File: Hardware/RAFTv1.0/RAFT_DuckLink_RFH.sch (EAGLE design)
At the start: 144 parts, among them J1 AMPHENOL_132134, J2 AMPHENOL_132134, J4 Micro-USB, J5 132134-15, J6 S2B-PH-K-S(LF)(SN), Q1 SIA817EDJ, Q2 SI7288DP, Q4 SI7288DP, U1 SX1276, U10 PE4259, U2 MAX2771ETI+, U3 ESP32-D0WD, U4 W25Q16BVSSIG, U5 INTERFACE-CP2102-GMR(QFN28), U6 PE4259, U7 SP0503BAHT, U8 BQ24650RVAR, U9 TPS63070RNMT, Y1 32.768kHz

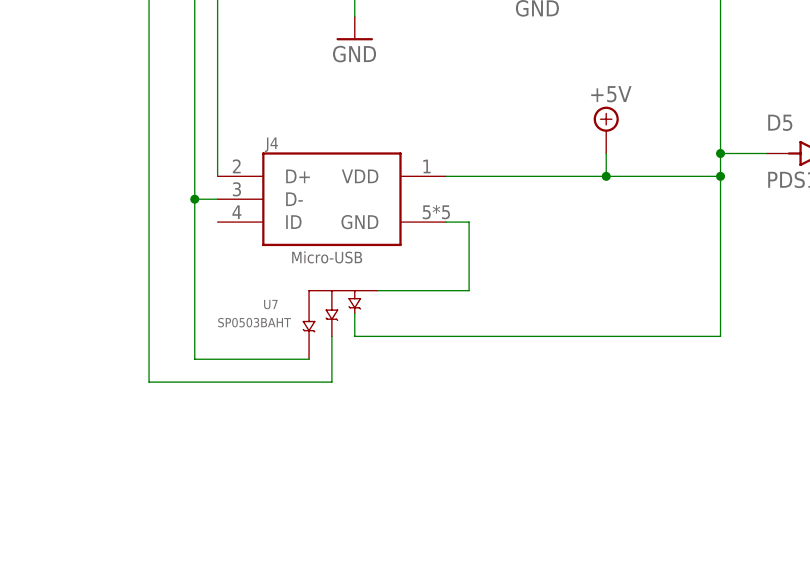
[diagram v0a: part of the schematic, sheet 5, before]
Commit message: added uart to board layout
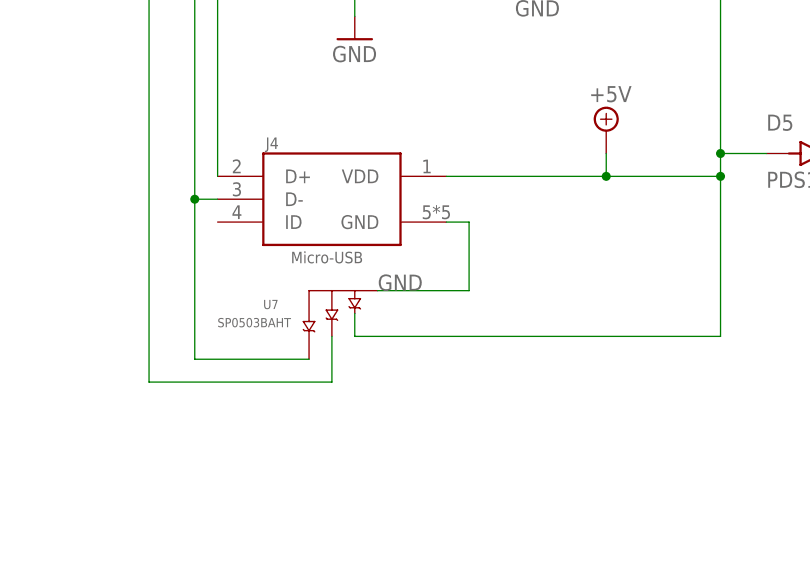
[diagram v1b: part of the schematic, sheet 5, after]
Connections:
- removed net N$56: J4.GND, U7.GND
- net GND: now also J4.GND, U7.GND
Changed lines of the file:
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@@
 <pinref part="R9" gate="G$1" pin="2"/>
+</segment>
+<segment>
+<pinref part="J4" gate="G$1" pin="GND"/>
+<wire x1="-2.54" y1="-38.1" x2="0" y2="-38.1" width="0.1524" layer="91"/>
+<pinref part="U7" gate="G$1" pin="GND"/>
+<wire x1="0" y1="-38.1" x2="0" y2="-45.72" width="0.1524" layer="91"/>
+<wire x1="0" y1="-45.72" x2="-10.16" y2="-45.72" width="0.1524" layer="91"/>
+<label x="-10.16" y="-45.72" size="1.778" layer="95"/>
 </segment>
 </net>
@@
 </segment>
 </net>
-<net name="N$56" class="0">
-<segment>
-<pinref part="J4" gate="G$1" pin="GND"/>
-<wire x1="-2.54" y1="-38.1" x2="0" y2="-38.1" width="0.1524" layer="91"/>
-<pinref part="U7" gate="G$1" pin="GND"/>
-<wire x1="0" y1="-38.1" x2="0" y2="-45.72" width="0.1524" layer="91"/>
-<wire x1="0" y1="-45.72" x2="-10.16" y2="-45.72" width="0.1524" layer="91"/>
-</segment>
-</net>

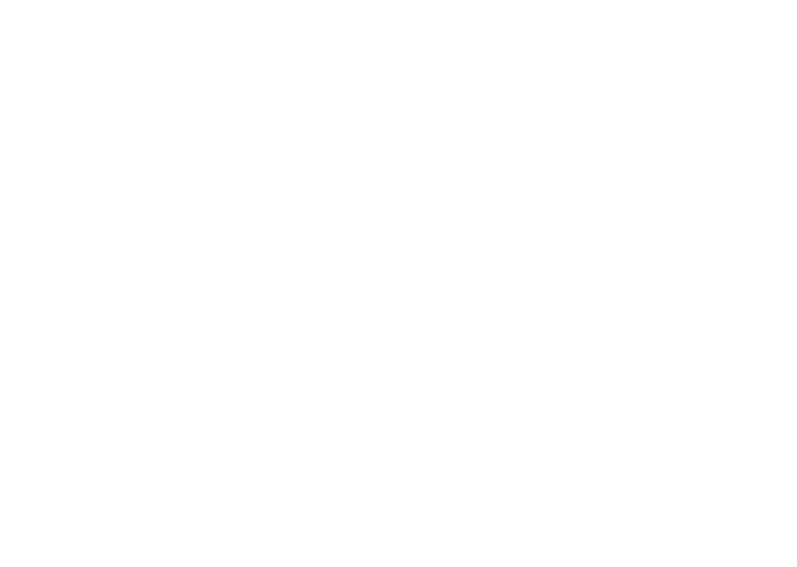
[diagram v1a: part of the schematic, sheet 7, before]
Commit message: added barrel jack. generated new PDFs
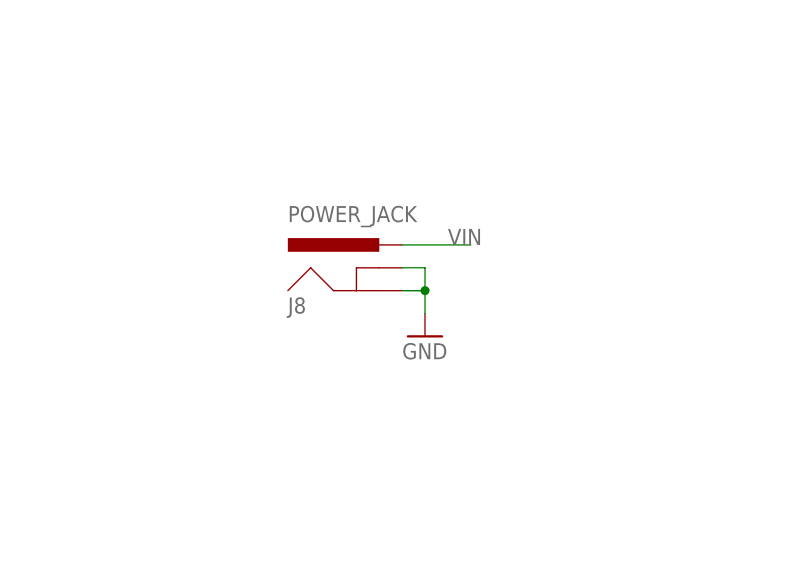
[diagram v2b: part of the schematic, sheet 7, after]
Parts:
- added J8: POWER_JACK, SparkFun-Connectors:POWER_JACK
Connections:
- net GND: now also J8.GND, J8.GNDBREAK
- net VIN: now also J8.PWR
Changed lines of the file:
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@@
 <part name="GND89" library="supply1" library_urn="urn:adsk.eagle:library:371" deviceset="GND" device=""/>
 <part name="D6" library="WL-SMCW" deviceset="WL-SMCW" device="-150060BS75000-B" value="150060RS75000"/>
+<part name="J8" library="SparkFun-Connectors" deviceset="POWER_JACK" device=""/>
+<part name="GND90" library="supply1" library_urn="urn:adsk.eagle:library:371" deviceset="GND" device=""/>
 </parts>
 <sheets>
@@
 </instance>
 <instance part="R14" gate="G$1" x="-104.14" y="33.02" smashed="yes" rot="R90">
-<attribute name="NAME" x="-97.277559375" y="36.06651875" size="2.54148125" layer="95" rot="R180"/>
-<attribute name="VALUE" x="-97.52603125" y="32.772640625" size="2.54331875" layer="96" rot="R180"/>
+<attribute name="NAME" x="-100.842440625" y="29.97348125" size="2.54148125" layer="95"/>
+<attribute name="VALUE" x="-100.59396875" y="33.267359375" size="2.54331875" layer="96"/>
 </instance>
 <instance part="R15" gate="G$1" x="-30.48" y="33.02" smashed="yes">
@@
 <attribute name="VALUE" x="45.72" y="38.1" size="1.778" layer="96"/>
 </instance>
+<instance part="J8" gate="G$1" x="-63.5" y="-55.88" smashed="yes">
+<attribute name="VALUE" x="-73.66" y="-45.72" size="1.778" layer="96" font="vector"/>
+<attribute name="NAME" x="-73.66" y="-55.88" size="1.778" layer="95" font="vector"/>
+</instance>
+<instance part="GND90" gate="1" x="-58.42" y="-58.42" smashed="yes">
+<attribute name="VALUE" x="-60.96" y="-60.96" size="1.778" layer="96"/>
+</instance>
 </instances>
 <busses>
@@
 <wire x1="71.12" y1="43.18" x2="48.26" y2="43.18" width="0.1524" layer="91"/>
 </segment>
+<segment>
+<pinref part="J8" gate="G$1" pin="GND"/>
+<pinref part="GND90" gate="1" pin="GND"/>
+<wire x1="-60.96" y1="-53.34" x2="-58.42" y2="-53.34" width="0.1524" layer="91"/>
+<wire x1="-58.42" y1="-53.34" x2="-58.42" y2="-55.88" width="0.1524" layer="91"/>
+<pinref part="J8" gate="G$1" pin="GNDBREAK"/>
+<wire x1="-60.96" y1="-50.8" x2="-58.42" y2="-50.8" width="0.1524" layer="91"/>
+<wire x1="-58.42" y1="-50.8" x2="-58.42" y2="-53.34" width="0.1524" layer="91"/>
+<junction x="-58.42" y="-53.34"/>
+</segment>
 </net>
 <net name="RTS" class="0">
@@
 </segment>
 </net>
+<net name="VIN" class="0">
+<segment>
+<pinref part="J8" gate="G$1" pin="PWR"/>
+<wire x1="-60.96" y1="-48.26" x2="-53.34" y2="-48.26" width="0.1524" layer="91"/>
+<label x="-55.88" y="-48.26" size="1.778" layer="95"/>
+</segment>
+</net>

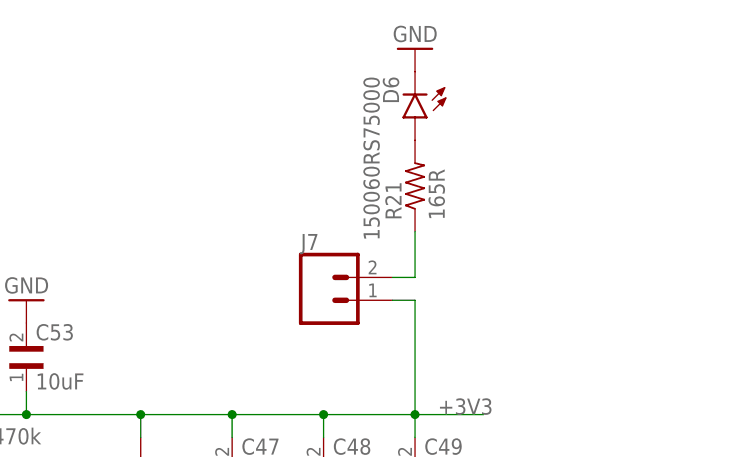
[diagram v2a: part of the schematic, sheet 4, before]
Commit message: battery charger/power distribution layouts
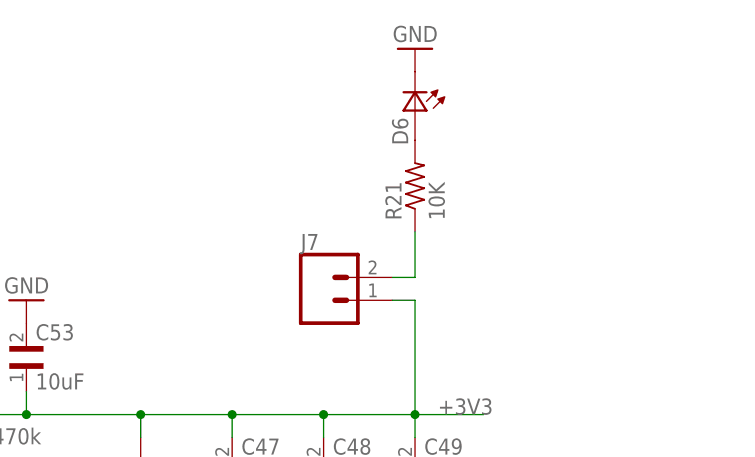
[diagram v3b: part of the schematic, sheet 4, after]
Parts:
- D6: value 150060RS75000 -> LTST-C190GKT; device WL-SMCW:WL-SMCW-150060BS75000-B -> LTST-C190GKT:LTST-C190GKT
- R21: value 165R -> 10K; device RAFT-components:CRCW1206165RFKEA -> CRCW040210K0JNED:CRCW040210K0JNED
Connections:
- net GND: now also D6.K2; no longer D6.C
- net N$52: now also D6.A2; no longer D6.A
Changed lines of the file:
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@@
 <part name="GND88" library="supply1" library_urn="urn:adsk.eagle:library:371" deviceset="GND" device=""/>
 <part name="J7" library="SparkFun-Connectors" deviceset="CONN_02" device=""/>
-<part name="R21" library="RAFT-components" deviceset="CRCW1206165RFKEA" device="" value="165R"/>
 <part name="GND89" library="supply1" library_urn="urn:adsk.eagle:library:371" deviceset="GND" device=""/>
-<part name="D6" library="WL-SMCW" deviceset="WL-SMCW" device="-150060BS75000-B" value="150060RS75000"/>
 <part name="J8" library="SparkFun-Connectors" deviceset="POWER_JACK" device=""/>
 <part name="GND90" library="supply1" library_urn="urn:adsk.eagle:library:371" deviceset="GND" device=""/>
+<part name="R21" library="CRCW040210K0JNED" deviceset="CRCW040210K0JNED" device="" value="10K"/>
+<part name="D6" library="LTST-C190GKT" deviceset="LTST-C190GKT" device=""/>
 </parts>
 <sheets>
@@
 <attribute name="NAME" x="71.12" y="28.448" size="1.778" layer="95" font="vector"/>
 </instance>
+<instance part="GND89" gate="1" x="83.82" y="50.8" smashed="yes" rot="R180">
+<attribute name="VALUE" x="86.36" y="53.34" size="1.778" layer="96" rot="R180"/>
+</instance>
 <instance part="R21" gate="G$1" x="83.82" y="35.56" smashed="yes" rot="R90">
 <attribute name="NAME" x="82.3214" y="31.75" size="1.778" layer="95" rot="R90"/>
 <attribute name="VALUE" x="87.122" y="31.75" size="1.778" layer="96" rot="R90"/>
 </instance>
-<instance part="GND89" gate="1" x="83.82" y="50.8" smashed="yes" rot="R180">
-<attribute name="VALUE" x="86.36" y="53.34" size="1.778" layer="96" rot="R180"/>
-</instance>
-<instance part="D6" gate="G$1" x="83.82" y="43.18" smashed="yes" rot="R180">
-<attribute name="NAME" x="80.264" y="47.752" size="1.778" layer="95" rot="R270"/>
-<attribute name="VALUE" x="78.105" y="47.752" size="1.778" layer="96" rot="R270"/>
+<instance part="D6" gate="G$1" x="83.82" y="45.72" smashed="yes" rot="R180">
+<attribute name="NAME" x="81.28203125" y="43.17796875" size="1.77941875" layer="95" rot="R270"/>
 </instance>
 </instances>
@@
 </segment>
 <segment>
+<pinref part="D6" gate="G$1" pin="K2"/>
 <pinref part="GND89" gate="1" pin="GND"/>
-<pinref part="D6" gate="G$1" pin="C"/>
 </segment>
 </net>
@@
 <pinref part="J7" gate="G$1" pin="2"/>
 <wire x1="81.28" y1="25.4" x2="83.82" y2="25.4" width="0.1524" layer="91"/>
+<wire x1="83.82" y1="25.4" x2="83.82" y2="30.48" width="0.1524" layer="91"/>
 <pinref part="R21" gate="G$1" pin="1"/>
-<wire x1="83.82" y1="25.4" x2="83.82" y2="30.48" width="0.1524" layer="91"/>
 </segment>
 </net>
 <net name="N$52" class="0">
 <segment>
+<pinref part="D6" gate="G$1" pin="A2"/>
 <pinref part="R21" gate="G$1" pin="2"/>
-<pinref part="D6" gate="G$1" pin="A"/>
-</segment>
-</net>
+</segment>
+</net>

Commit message: preliminary board layout
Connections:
- net 2G4_INT_ANT: now also U10.RF2; no longer U10.RF1
- net N$70: now also U10.RF1; no longer U10.RF2
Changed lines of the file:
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@@
-</segment>
-</net>
-<net name="2G4_INT_ANT" class="0">
-<segment>
-<wire x1="-190.5" y1="-50.8" x2="-213.36" y2="-50.8" width="0.1524" layer="91"/>
-<label x="-213.36" y="-50.8" size="1.778" layer="95"/>
-<pinref part="U10" gate="G$1" pin="RF1"/>
 </segment>
 </net>
@@
 <net name="N$70" class="0">
 <segment>
-<wire x1="-190.5" y1="-53.34" x2="-195.58" y2="-53.34" width="0.1524" layer="91"/>
-<wire x1="-195.58" y1="-53.34" x2="-195.58" y2="-58.42" width="0.1524" layer="91"/>
 <pinref part="J5" gate="G$1" pin="SIG"/>
 <wire x1="-195.58" y1="-58.42" x2="-205.74" y2="-58.42" width="0.1524" layer="91"/>
-<pinref part="U10" gate="G$1" pin="RF2"/>
+<pinref part="U10" gate="G$1" pin="RF1"/>
+<wire x1="-190.5" y1="-50.8" x2="-195.58" y2="-50.8" width="0.1524" layer="91"/>
+<wire x1="-195.58" y1="-50.8" x2="-195.58" y2="-58.42" width="0.1524" layer="91"/>
 </segment>
 </net>
@@
 </segment>
 </net>
+<net name="2G4_INT_ANT" class="0">
+<segment>
+<pinref part="U10" gate="G$1" pin="RF2"/>
+<wire x1="-190.5" y1="-53.34" x2="-190.5" y2="-86.36" width="0.1524" layer="91"/>
+<wire x1="-190.5" y1="-86.36" x2="-213.36" y2="-86.36" width="0.1524" layer="91"/>
+<label x="-213.36" y="-86.36" size="1.778" layer="95"/>
+</segment>
+</net>

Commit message: mostly good board design
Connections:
- net +3.3V: now also J3.16, J3.18
- net +3V3: no longer J3.16, J3.18
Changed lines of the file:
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@@
-</segment>
-</net>
-<net name="+3V3" class="0">
-<segment>
-<wire x1="96.52" y1="-5.08" x2="78.74" y2="-5.08" width="0.1524" layer="91"/>
-<pinref part="J3" gate="G$1" pin="18"/>
-<label x="88.9" y="-5.08" size="1.778" layer="95"/>
-</segment>
-<segment>
-<wire x1="96.52" y1="-2.54" x2="78.74" y2="-2.54" width="0.1524" layer="91"/>
-<pinref part="J3" gate="G$1" pin="16"/>
-<label x="88.9" y="-2.54" size="1.778" layer="95"/>
 </segment>
 </net>
@@
 </segment>
 </net>
+<net name="+3.3V" class="0">
+<segment>
+<wire x1="96.52" y1="-2.54" x2="78.74" y2="-2.54" width="0.1524" layer="91"/>
+<pinref part="J3" gate="G$1" pin="16"/>
+<label x="88.9" y="-2.54" size="1.778" layer="95"/>
+</segment>
+<segment>
+<wire x1="96.52" y1="-5.08" x2="78.74" y2="-5.08" width="0.1524" layer="91"/>
+<pinref part="J3" gate="G$1" pin="18"/>
+<label x="88.9" y="-5.08" size="1.778" layer="95"/>
+</segment>
+</net>
